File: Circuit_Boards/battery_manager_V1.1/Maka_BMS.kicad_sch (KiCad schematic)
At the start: 95 parts, among them J8 ‎SAM16035-ND‎, J9 Molex 087340-1424, Q1 FDC645N, Q2 FDC645N, Q3 FDC645N, Q4 Si3483CDV, Q5 Si3483CDV, Q6 FDC645N, U1 AP63205, U2 TPS70933DBV, U3 BQ77915, U4 LTC6994CS6-1, U5 LTC4007, U6 MP3213, U7 TPS70933DBV, U8 MCP3221

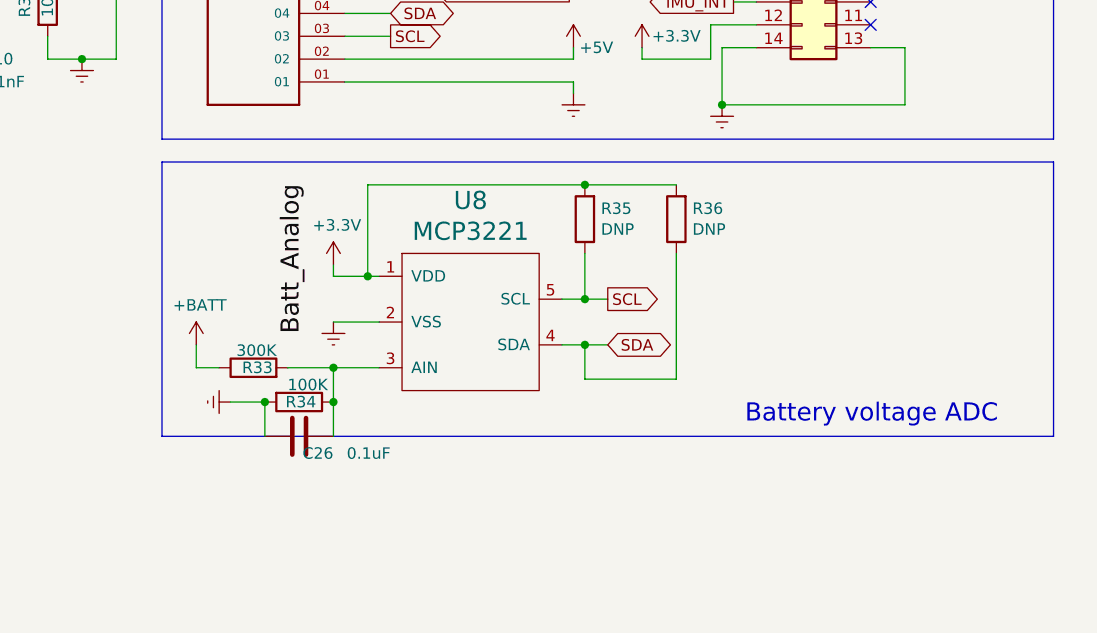
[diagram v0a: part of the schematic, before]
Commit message: cleaned up a bit and mainly added the LED board to the repo
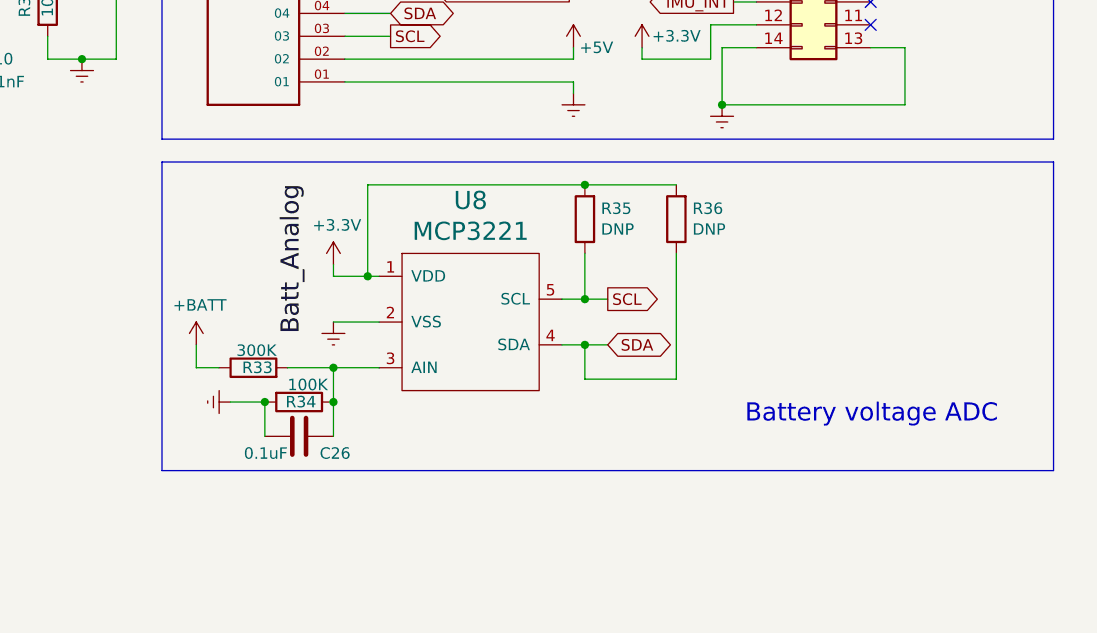
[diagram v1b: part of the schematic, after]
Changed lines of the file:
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@@
     (stroke (width 0) (type default) (color 0 0 0 0))
   )
-  (polyline (pts (xy 184.15 130.81) (xy 184.15 161.29))
+  (polyline (pts (xy 184.15 130.81) (xy 184.15 165.1))
     (stroke (width 0) (type default) (color 0 0 0 0))
   )
@@
     (stroke (width 0) (type default) (color 0 0 0 0))
   )
-  (polyline (pts (xy 184.15 161.29) (xy 283.21 161.29))
+  (polyline (pts (xy 184.15 165.1) (xy 283.21 165.1))
     (stroke (width 0) (type default) (color 0 0 0 0))
   )
@@
     (stroke (width 0) (type default) (color 0 0 0 0))
   )
-  (polyline (pts (xy 283.21 161.29) (xy 283.21 130.81))
+  (polyline (pts (xy 283.21 165.1) (xy 283.21 130.81))
     (stroke (width 0) (type default) (color 0 0 0 0))
   )
@@
   (symbol (lib_id "Device:C") (at 199.39 161.29 270) (unit 1)
     (in_bom yes) (on_board yes)
-    (property "Reference" "C26" (id 0) (at 203.2 163.195 90)
+    (property "Reference" "C26" (id 0) (at 205.105 163.195 90)
       (effects (font (size 1.27 1.27)) (justify right))
     )
-    (property "Value" "0.1uF" (id 1) (at 209.55 163.195 90)
+    (property "Value" "0.1uF" (id 1) (at 198.12 163.195 90)
       (effects (font (size 1.27 1.27)) (justify right))
     )

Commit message: removed BOM and gerbers for kicad project, to ensure up to date exports
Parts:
- 0.0, 7.4_1, 7.4_2, U8: Buy Digikey Buy -> (none)
- 11.1, 12V_OUT1, 3.4, C1, C10, C11, C12, C13, C14, C15, C16, C17, C18, C19, C2, C20, C21, C22, C23, C24, C25, C26, C3, C4, C5, C6, C7, C8, C9, D1, D2, D3, D4, GND_OUT1, L1, L2, L3, R1, R10, R11, R12, R13, R14, R15, R16, R17, R18, R19, R2, R20, R21, R22, R23, R24, R25, R26, R27, R28, R29, R3, R30, R31, R32, R33, R34, R35, R36, R37, R4, R5, R6, R7, R8, R9, TH1, TH2: Buy Digikey skip -> (none)
- J8: Buy Digikey skip: SAMTEC -> (none)
- J9: Buy Digikey Buy: limited -> (none)
- Q1, Q2, Q3, Q4, Q5, Q6: Buy Digikey Buy: Substitute -> (none)
- U1, U3, U4, U5: Buy Digikey Buy: No stock -> (none)
- U2, U7: Buy Digikey Buy: substitute -> (none)
- U6: Buy Digikey Buy: Mouser -> (none)
